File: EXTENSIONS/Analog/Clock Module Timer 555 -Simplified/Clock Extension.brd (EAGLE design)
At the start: 48 x 38 mm, 12 parts, among them Q1 2N3906, T555_CLOCK NE555N, X1 USB-A

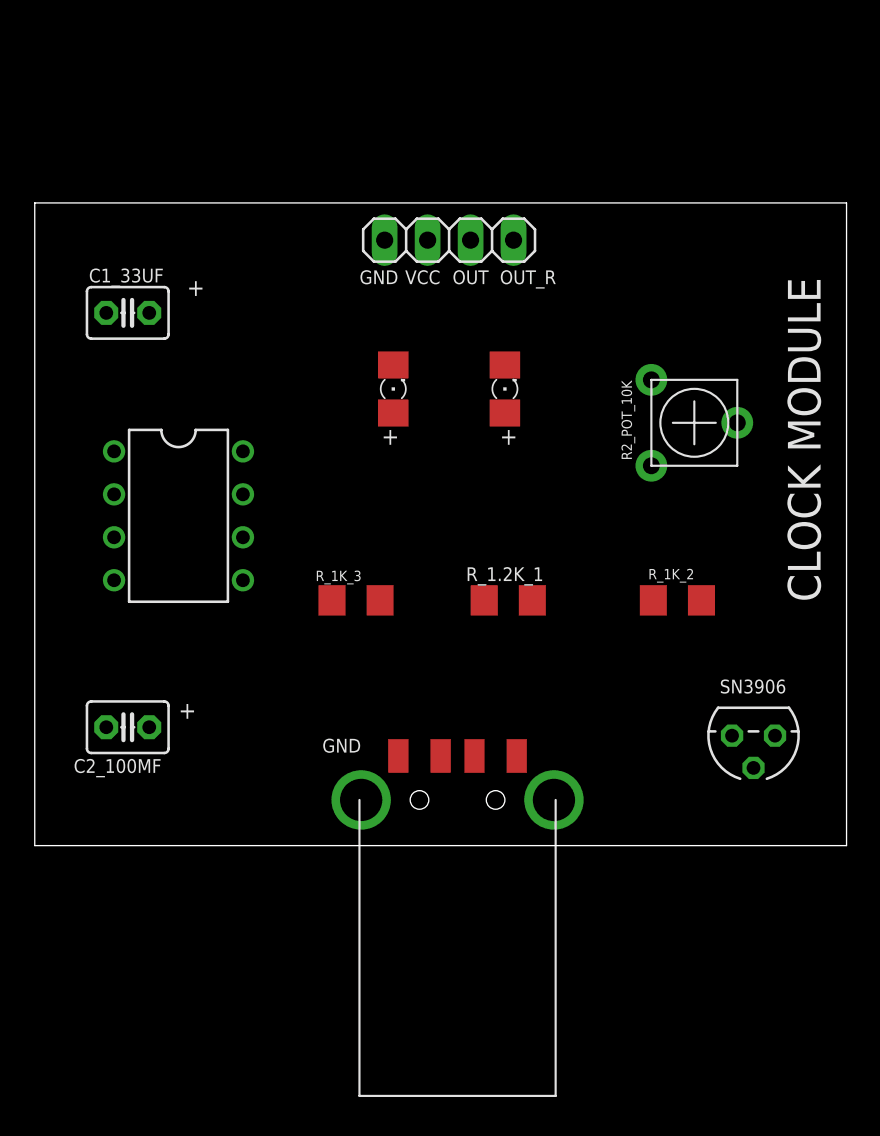
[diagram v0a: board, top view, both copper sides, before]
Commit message: Update/create Clock Module Time 555 -Simplified
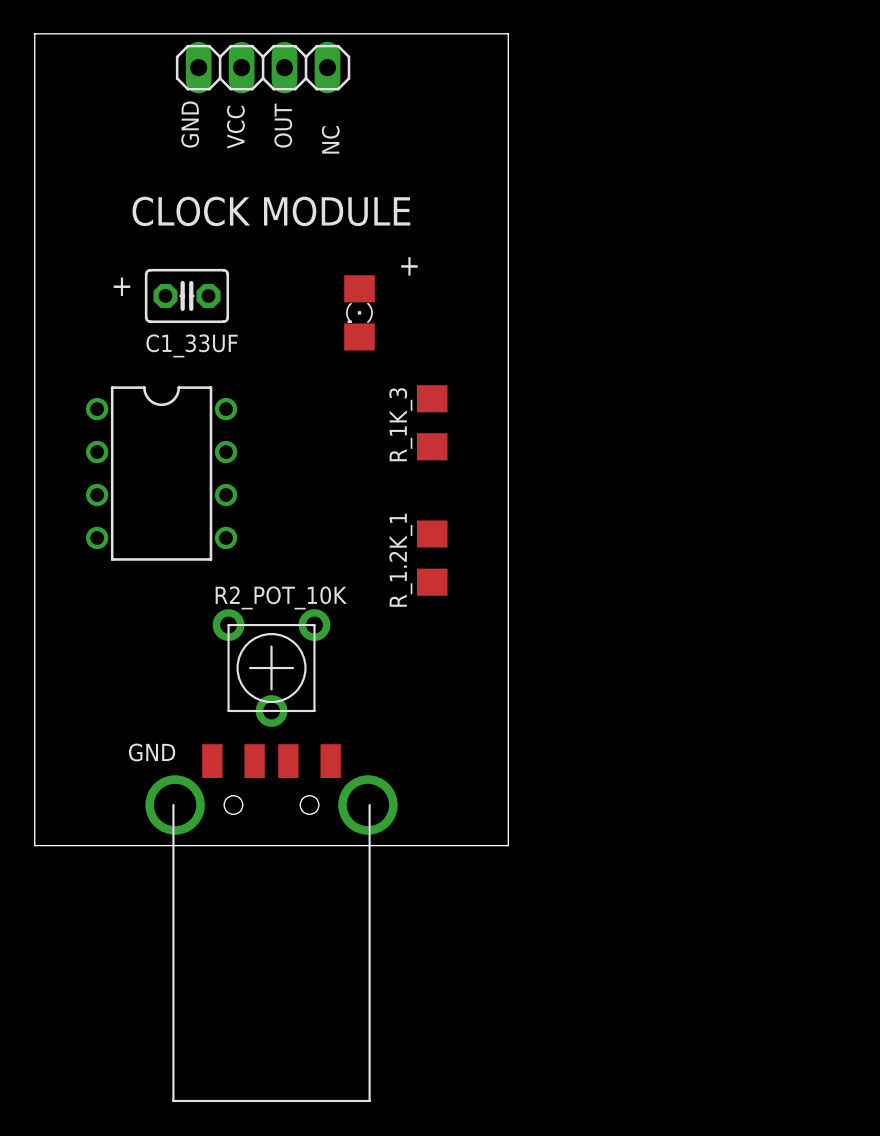
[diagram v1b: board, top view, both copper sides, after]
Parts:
- removed C2_100MF: (no value), adafruit:C025-030X050
- removed LED_OUTPUT_REVERSE: (no value), adafruit:1206
- removed Q1: 2N3906, transistor-pnp:TO92
- removed R_1K_2: (no value), adafruit:R1206
- moved R2_POT_10K 28.9 mm to (16.0, 22.5), turned to 180 degrees
- moved JP1 15.0 mm to (15.5, 58.0)
- moved R_1K_3 11.4 mm to (25.5, 37.0), turned to 90 degrees
- moved X1 11.0 mm to (16.0, 14.4)
- moved R_1.2K_1 5.15 mm to (25.5, 29.0), turned to 90 degrees
- moved LED_OUTPUT 4.92 mm to (21.2, 43.5), turned to 270 degrees
- moved C1_33UF 3.64 mm to (11.0, 44.5), turned to 180 degrees
- moved T555_CLOCK 2.69 mm to (9.50, 34.0)
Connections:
- removed net N$6: LED_OUTPUT_REVERSE.C, R_1K_2.2
- net GND: no longer C2_100MF.1
- net TMR555_OUTPUT: no longer Q1.2
- net TMR555_OUTPUT_REVERSE: no longer Q1.3, R_1K_2.1
- net VCC: no longer C2_100MF.2, LED_OUTPUT_REVERSE.A
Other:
- board size 48 x 38 mm -> 28 x 48 mm
- board text added: "NC"
- board text added: "PCBv3 - 2019.08"
- board text removed: "OUT_R"
- board text removed: "PCBv2 - 2017.08"
- board text removed: "SN3906"

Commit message: fix bug in pcb '0 TO 9 Counter 74LS90'
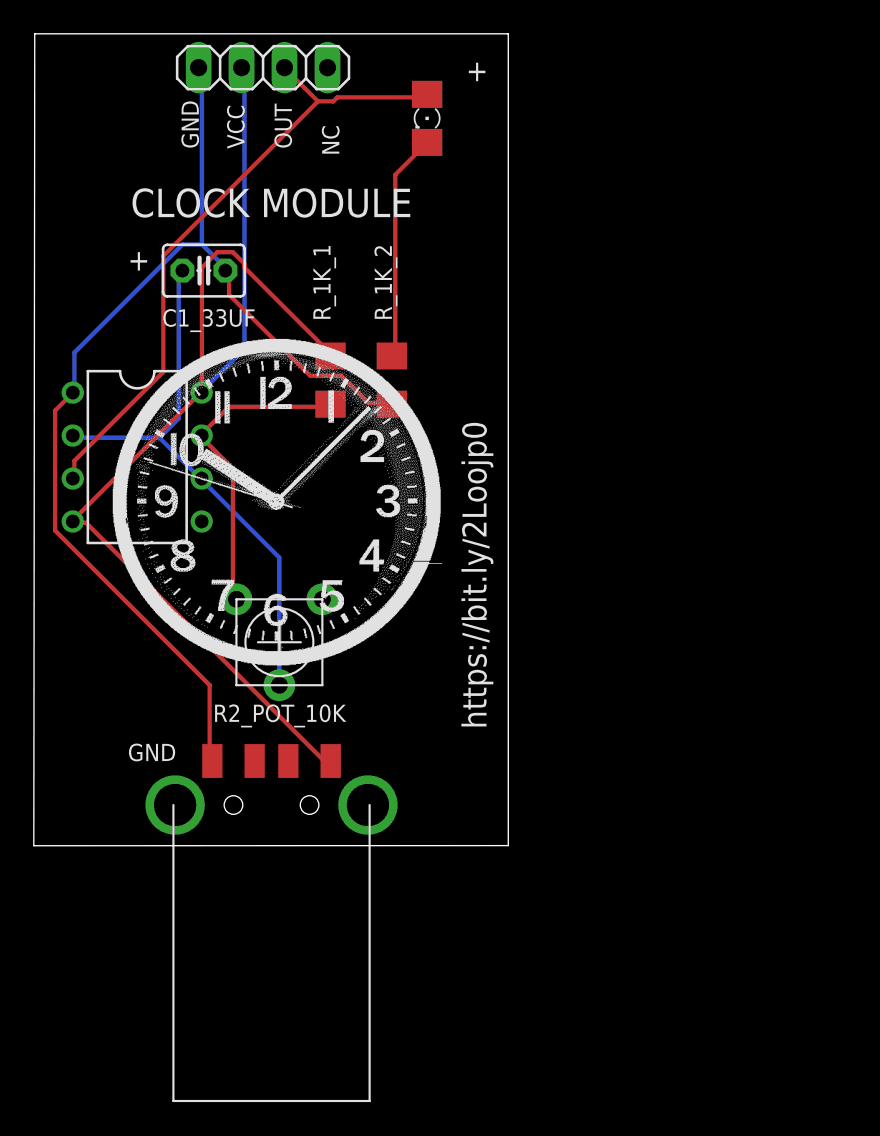
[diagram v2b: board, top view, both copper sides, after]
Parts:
- removed R_1.2K_1, R_1K_3: (no value), adafruit:R1206
- added R_1K_1, R_1K_2: (no value), adafruit:R1206
- moved LED_OUTPUT 12.2 mm to (25.2, 55.0)
- moved C1_33UF 1.80 mm to (12.0, 46.0)
- moved T555_CLOCK 1.74 mm to (8.06, 35.0)
- moved R2_POT_10K 1.59 mm to (16.5, 24.0)
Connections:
- net GND: now also R_1K_2.1; no longer R_1K_3.1
- net N$1: now also R_1K_1.1; no longer R_1.2K_1.1
- net N$5: now also R_1K_2.2; no longer R_1K_3.2
- net VCC: now also R_1K_1.2; no longer R_1.2K_1.2
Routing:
- net VCC: track 0.00 -> 70.4 mm
- net GND: track 0.00 -> 65.3 mm
- net TMR555_OUTPUT: track 0.00 -> 37.8 mm
- net THRESHOLD: track 0.00 -> 33.3 mm
- net N$1: track 0.00 -> 19.0 mm
- net N$5: track 0.00 -> 13.5 mm
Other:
- board size 28 x 48 mm -> 28.1 x 48 mm
- board text added: "https://bit.ly/2Loojp0"
